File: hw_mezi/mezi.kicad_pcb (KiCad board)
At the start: 2 copper layers, 45.4 x 54.7 mm, 42 parts, among them J1 Conn_2Rows-05Pins, Q1 AO3401A, Q2 AO3401A, Q3 AO3401A, SW1 SW_DPST_x2, T1 Tab, U1 PY32F002AF15P6TU

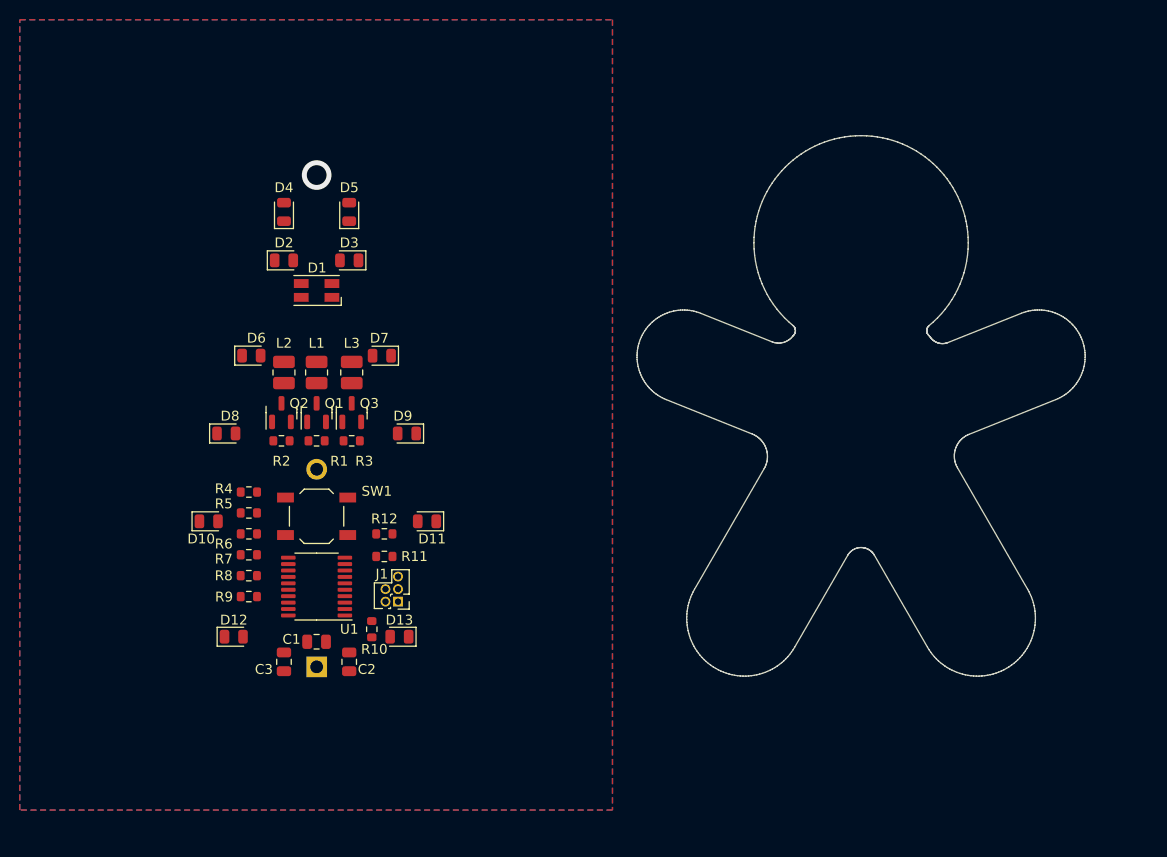
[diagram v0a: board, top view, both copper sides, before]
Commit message: Hoember + Mezi routed
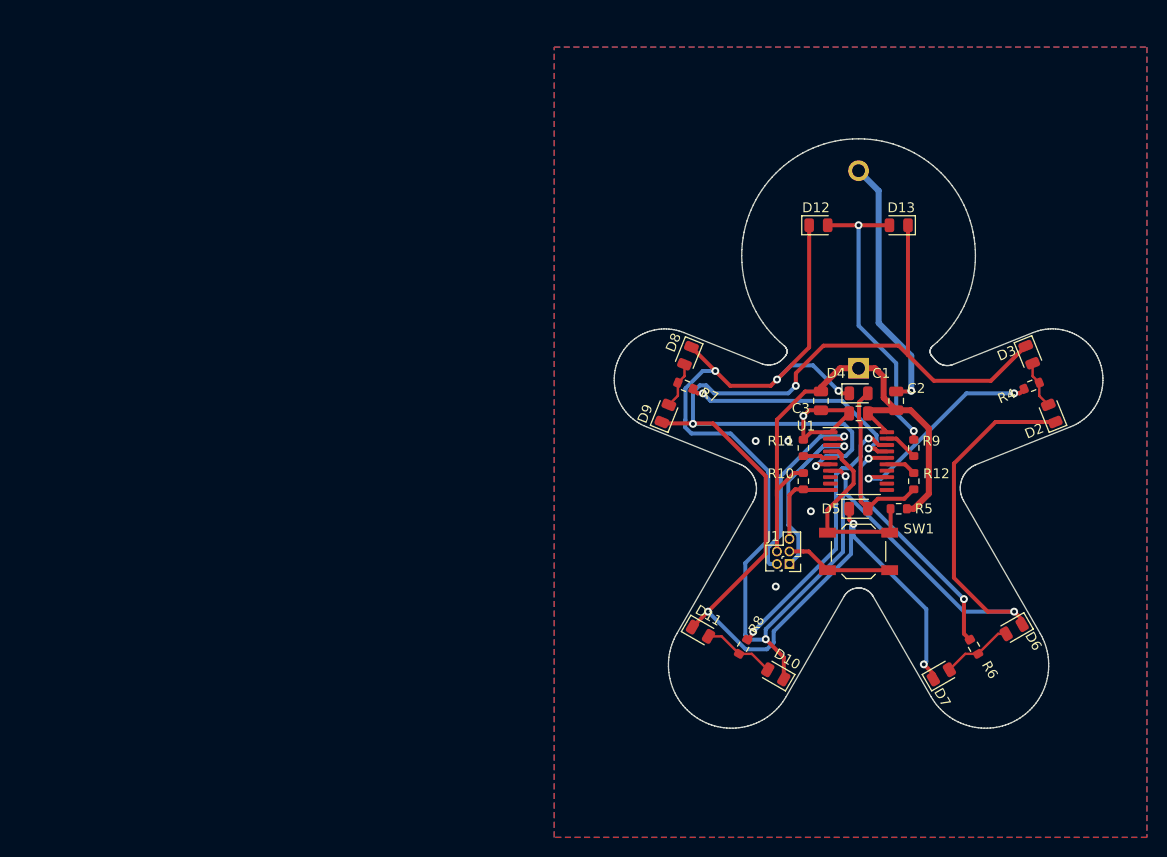
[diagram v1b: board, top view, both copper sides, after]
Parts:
- removed D1: LED_ARGB, LED_SMD:LED_RGB_Wuerth-PLCC4_3.2x2.8mm_150141M173100
- removed L1, L2, L3: L, Inductor_SMD:L_1008_2520Metric
- removed Q1, Q2, Q3: AO3401A, sajat:SOT-23
- removed R1, R2, R3: 100k, Resistor_SMD:R_0603_1608Metric
- moved D6 82.0 mm to (200.7, 91.7), turned to -150 degrees
- moved R4 80.0 mm to (202.4, 67.1), turned to -158 degrees
- moved D2 79.3 mm to (204.5, 69.8), turned to 112 degrees
- moved R6 74.3 mm to (196.6, 93.5), turned to 120 degrees
- moved D12 72.4 mm to (180.8, 50.8)
- moved D3 69.5 mm to (202.2, 63.9), turned to -68 degrees
- moved R9 69.0 mm to (190.5, 73.3), turned to -90 degrees
- moved R5 67.4 mm to (190.5, 76.7), turned to 90 degrees
- moved D13 65.5 mm to (189.0, 50.8)
- moved D7 65.2 mm to (193.3, 96.3), turned to 30 degrees
- moved BT1 62.6 mm to (184.9, 65.3)
- moved C2 61.4 mm to (188.7, 68.6), turned to 90 degrees
- moved D4 61.0 mm to (184.9, 67.8), turned to 0 degrees
- moved C3 60.4 mm to (181.1, 68.6)
- moved D5 59.7 mm to (184.9, 79.5), turned to 0 degrees
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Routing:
- net /MPX1: track 0.00 -> 156.4 mm, vias 0 -> 6
- net /MPX2: track 0.00 -> 155.6 mm, vias 0 -> 6
- net VCC: track 0.00 -> 54.0 mm
- net GND: track 0.00 -> 50.0 mm, vias 1 -> 6
- net Net-(D12-A): track 0.00 -> 30.3 mm, vias 0 -> 2
- net /L5: track 0.00 -> 28.0 mm, vias 0 -> 2
- net /L3: track 0.00 -> 25.1 mm, vias 0 -> 2
- net /L4: track 0.00 -> 24.2 mm, vias 0 -> 2
- net /L1: track 0.00 -> 21.4 mm, vias 0 -> 2
- net /SWD: track 0.00 -> 19.8 mm, vias 0 -> 1
- net Net-(SW1A-A): track 0.00 -> 19.6 mm
- net Net-(D4-A): track 0.00 -> 17.9 mm
- net /SWC: track 0.00 -> 17.8 mm, vias 0 -> 1
- net /nRST: track 0.00 -> 8.84 mm
- net Net-(D10-A): track 0.00 -> 7.40 mm
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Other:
- board size 45.4 x 54.7 mm -> 49.5 x 59.7 mm

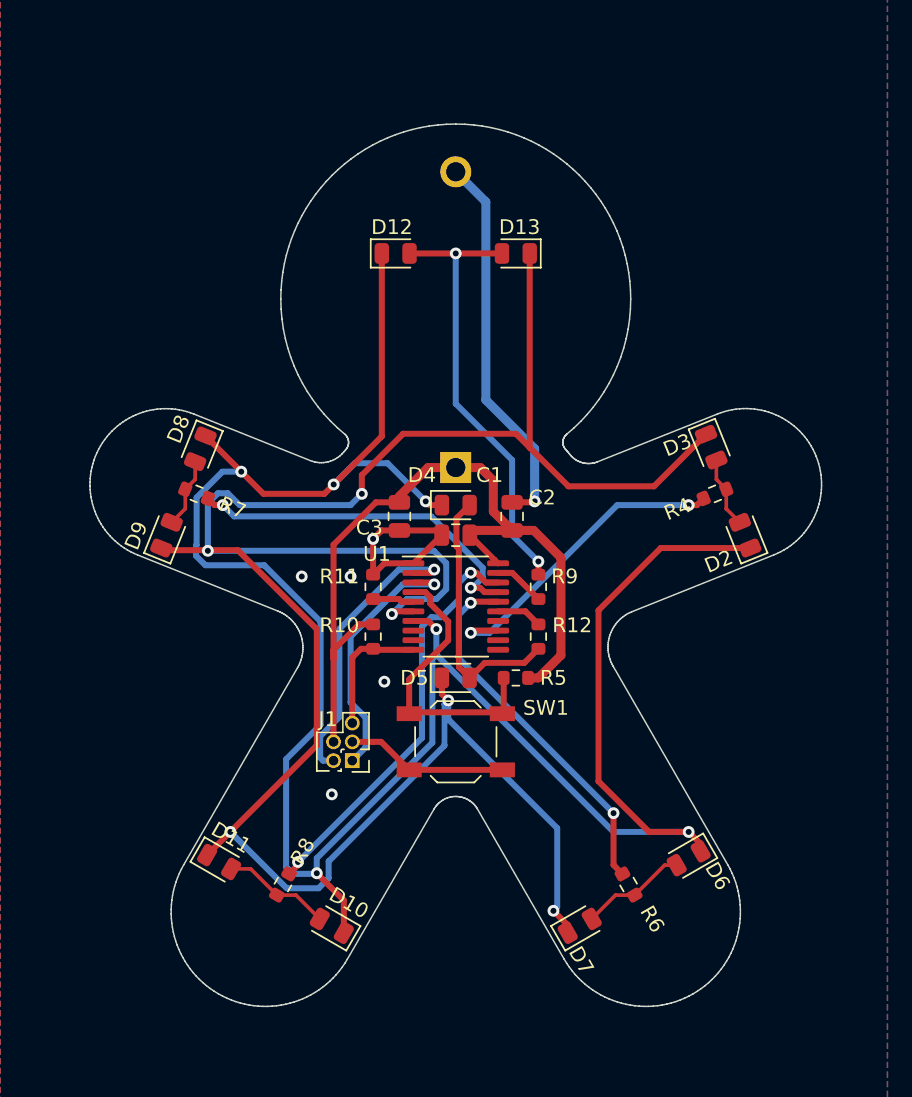
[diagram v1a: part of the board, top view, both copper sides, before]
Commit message: mezi tssop JLC swap + hole on top
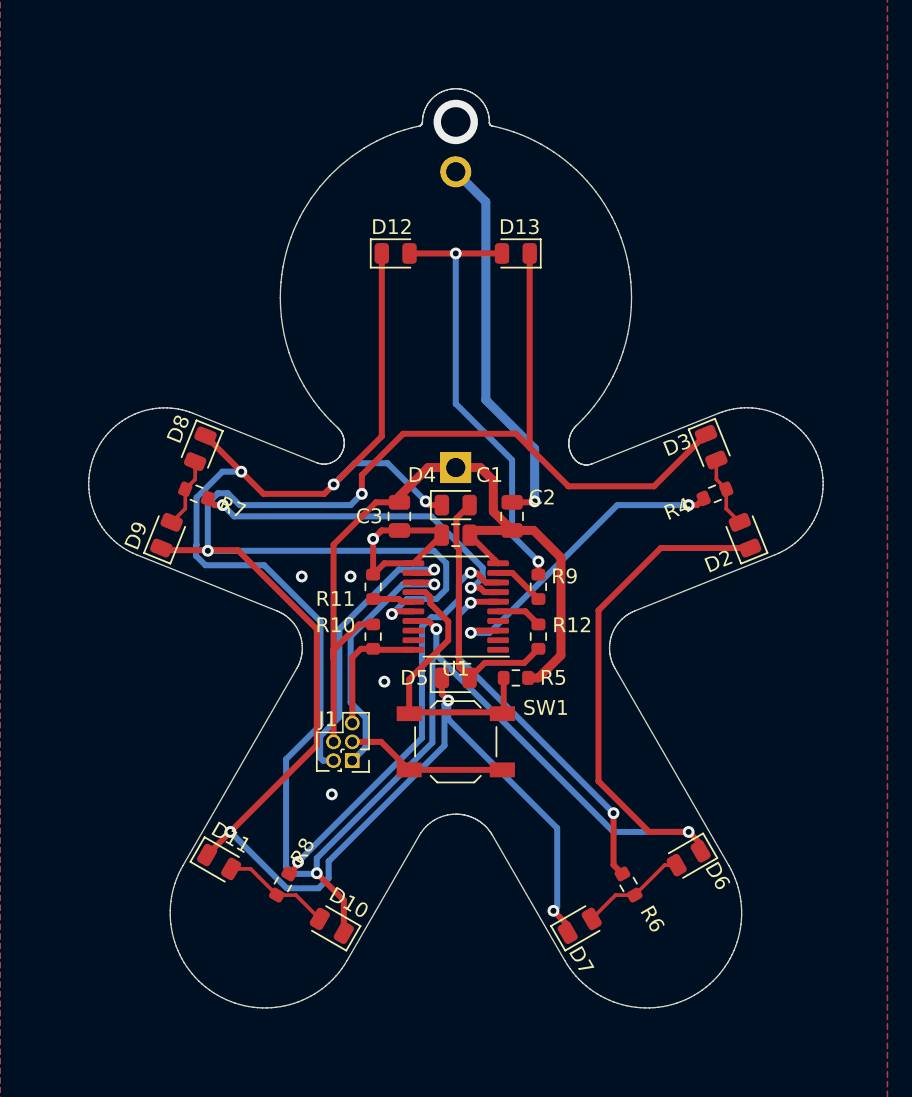
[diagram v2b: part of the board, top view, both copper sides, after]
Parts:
- U1: footprint Package_SO:TSSOP-20_4.4x6.5mm_P0.65mm -> karifa:TSSOP-20_4.4x6.5mm_P0.65mm
- moved T1 13.3 mm to (171.4, 102.1)
- moved T1 3.80 mm to (170.4, 85.1)
- moved T1 2.81 mm to (199.4, 84.8)
- moved T1 2.32 mm to (184.9, 39.4)
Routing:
- net GND: vias 6 -> 7
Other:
- board size 49.5 x 59.7 mm -> 49.7 x 62.2 mm

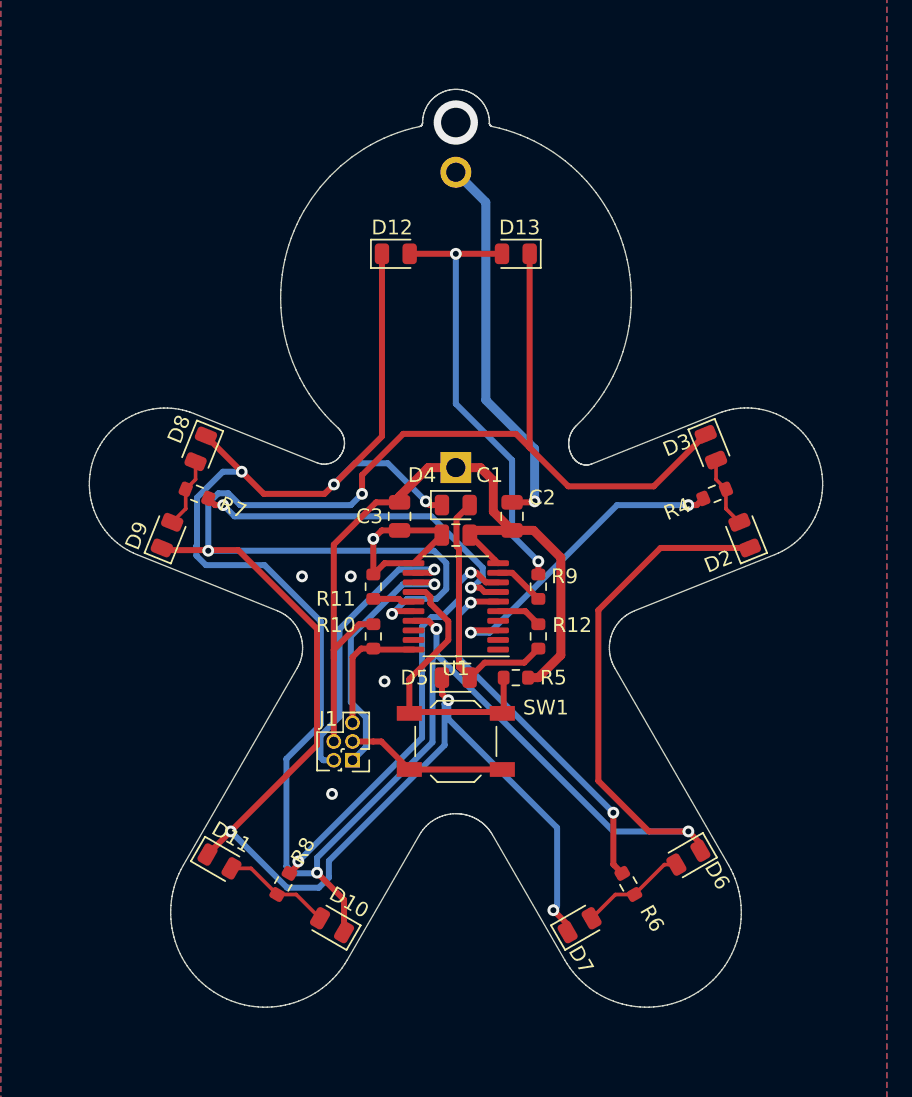
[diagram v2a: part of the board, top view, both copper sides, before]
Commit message: Added hoember and mezi panel
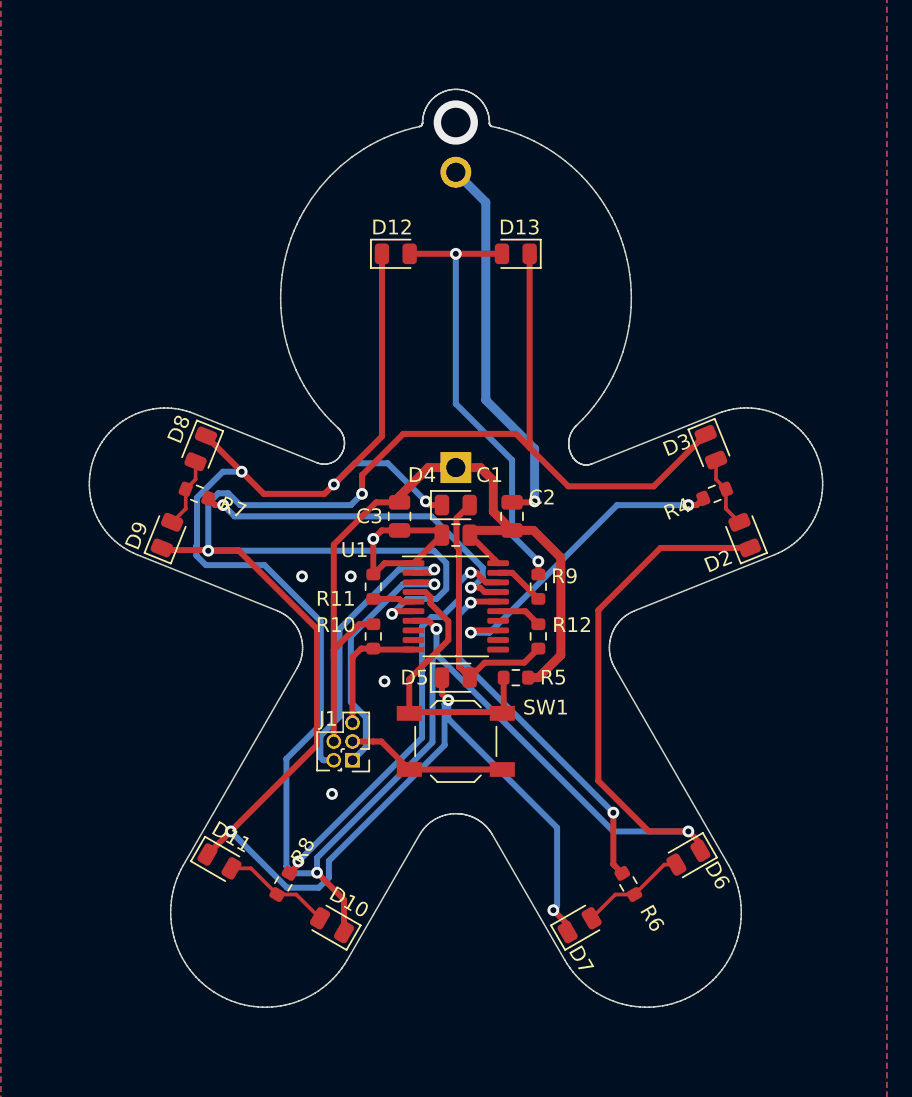
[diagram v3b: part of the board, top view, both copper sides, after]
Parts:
- removed the T1 at (199.4, 84.8)
- removed the T1 at (184.9, 39.4)
- added T1: Tab, kikit:Tab, F.Cu at (204.2, 88.9)
- added T53,086: Tab, kikit:Tab, F.Cu at (198.9, 52.8)
- moved T1 32.3 mm to (171.4, 52.8)
- moved T1 14.8 mm to (164.8, 88.9), turned to 0 degrees
- turned U1 to 180 degrees
